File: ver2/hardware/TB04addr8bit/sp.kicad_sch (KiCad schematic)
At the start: 7 parts, among them U32 74AHC04, U39 74HC193, U40 74HC00, U41 74LS32, U42 74AHC04, U43 74LS08

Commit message: ver2: レジスタファイル(RS00/RS01)とルート配線・発振回路定数を追加
- clk_rst: 74HC4060発振のRf=10M/Rs=220K/C=22p×2に確定
- RS00/RS01: R0-R7の具体回路(74HC161×4+74LS253×4)を追加
  ※図面は74LS253だがシンボル都合で実装はHC(74HC253)
- ルート: 書込デコード/読出セレクト/RegAddrSrc MUX/データ入出力の
  外側グルーを配線(DI/DOa/DOb/Reg_WE0-7/sel_a)
- PC_mAddrは作業中(Reg_WE8-11未結線)

Co-Authored-By: Claude Opus 4.8 <noreply@anthropic.com>
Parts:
- removed U32: 74AHC04, symbol 74xx:74AHC04
- removed unit 1 of U42
- added U16: 74HC00, Package_DIP:DIP-14_W7.62mm_Socket, symbol 74xx:74HC00
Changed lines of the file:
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@@
+	)
+	(symbol
+		(lib_id "74xx:74HC00")
+		(at 205.74 147.32 0)
+		(mirror y)
+		(unit 2)
+		(body_style 1)
+		(exclude_from_sim no)
+		(in_bom yes)
+		(on_board yes)
+		(in_pos_files yes)
+		(dnp no)
+		(property "Reference" "U16"
+			(at 205.7483 138.43 0)
+			(show_name no)
+			(do_not_autoplace no)
+			(effects
+				(font
+					(size 1.27 1.27)
+				)
+			)
+		)
+		(property "Value" "74HC00"
+			(at 205.7483 140.97 0)
+			(show_name no)
+			(do_not_autoplace no)
+			(effects
+				(font
+					(size 1.27 1.27)
+				)
+			)
+		)
+		(property "Footprint" "Package_DIP:DIP-14_W7.62mm_Socket"
+			(at 205.74 147.32 0)
+			(hide yes)
+			(show_name no)
+			(do_not_autoplace no)
+			(effects
+				(font
+					(size 1.27 1.27)
+				)
+			)
+		)
+		(property "Datasheet" "http://www.ti.com/lit/gpn/sn74hc00"
+			(at 205.74 147.32 0)
+			(hide yes)
+			(show_name no)
+			(do_not_autoplace no)
+			(effects
+				(font
+					(size 1.27 1.27)
+				)
+			)
+		)
+		(property "Description" "quad 2-input NAND gate"
+			(at 205.74 147.32 0)
+			(hide yes)
+			(show_name no)
+			(do_not_autoplace no)
+			(effects
+				(font
+					(size 1.27 1.27)
+				)
+			)
+		)
+		(pin "1"
+		)
+		(pin "2"
+		)
+		(pin "3"
+		)
+		(pin "9"
+		)
+		(pin "12"
+		)
+		(pin "4"
+		)
+		(pin "5"
+		)
+		(pin "6"
+		)
+		(pin "10"
+		)
+		(pin "8"
+		)
+		(pin "14"
+		)
+		(pin "7"
+		)
+		(pin "11"
+		)
+		(pin "13"
+		)
+		(instances
+			(project "TB04addr8bit"
+				(path "/d176c79b-dced-4d01-bcec-7dfd676fcfc2/49a9e3a4-2acb-465c-a9e5-4345d5d7643a"
+					(reference "U16")
+					(unit 2)
+				)
+			)
+		)
 	)
 	(symbol
@@
 	)
 	(symbol
+		(lib_id "74xx:74HC00")
+		(at 182.88 147.32 0)
+		(mirror y)
+		(unit 1)
+		(body_style 1)
+		(exclude_from_sim no)
+		(in_bom yes)
+		(on_board yes)
+		(in_pos_files yes)
+		(dnp no)
+		(property "Reference" "U16"
+			(at 182.8883 138.43 0)
+			(show_name no)
+			(do_not_autoplace no)
+			(effects
+				(font
+					(size 1.27 1.27)
+				)
+			)
+		)
+		(property "Value" "74HC00"
+			(at 182.8883 140.97 0)
+			(show_name no)
+			(do_not_autoplace no)
+			(effects
+				(font
+					(size 1.27 1.27)
+				)
+			)
+		)
+		(property "Footprint" "Package_DIP:DIP-14_W7.62mm_Socket"
+			(at 182.88 147.32 0)
+			(hide yes)
+			(show_name no)
+			(do_not_autoplace no)
+			(effects
+				(font
+					(size 1.27 1.27)
+				)
+			)
+		)
+		(property "Datasheet" "http://www.ti.com/lit/gpn/sn74hc00"
+			(at 182.88 147.32 0)
+			(hide yes)
+			(show_name no)
+			(do_not_autoplace no)
+			(effects
+				(font
+					(size 1.27 1.27)
+				)
+			)
+		)
+		(property "Description" "quad 2-input NAND gate"
+			(at 182.88 147.32 0)
+			(hide yes)
+			(show_name no)
+			(do_not_autoplace no)
+			(effects
+				(font
+					(size 1.27 1.27)
+				)
+			)
+		)
+		(pin "1"
+		)
+		(pin "2"
+		)
+		(pin "3"
+		)
+		(pin "9"
+		)
+		(pin "12"
+		)
+		(pin "4"
+		)
+		(pin "5"
+		)
+		(pin "6"
+		)
+		(pin "10"
+		)
+		(pin "8"
+		)
+		(pin "14"
+		)
+		(pin "7"
+		)
+		(pin "11"
+		)
+		(pin "13"
+		)
+		(instances
+			(project "TB04addr8bit"
+				(path "/d176c79b-dced-4d01-bcec-7dfd676fcfc2/49a9e3a4-2acb-465c-a9e5-4345d5d7643a"
+					(reference "U16")
+					(unit 1)
+				)
+			)
+		)
+	)
+	(symbol
 		(lib_id "74xx:74AHC04")
 		(at 276.86 63.5 0)
@@
 	)
 	(symbol
-		(lib_id "74xx:74AHC04")
-		(at 255.27 34.29 0)
-		(unit 1)
-		(body_style 1)
-		(exclude_from_sim no)
-		(in_bom yes)
-		(on_board yes)
-		(in_pos_files yes)
-		(dnp no)
-		(fields_autoplaced yes)
-		(property "Reference" "U42"
-			(at 255.27 25.4 0)
-			(show_name no)
-			(do_not_autoplace no)
-			(effects
-				(font
-					(size 1.27 1.27)
-				)
-			)
-		)
-		(property "Value" "74AHC04"
-			(at 255.27 27.94 0)
-			(show_name no)
-			(do_not_autoplace no)
-			(effects
-				(font
-					(size 1.27 1.27)
-				)
-			)
-		)
-		(property "Footprint" ""
-			(at 255.27 34.29 0)
-			(hide yes)
-			(show_name no)
-			(do_not_autoplace no)
-			(effects
-				(font
-					(size 1.27 1.27)
-				)
-			)
-		)
-		(property "Datasheet" "https://assets.nexperia.com/documents/data-sheet/74AHC_AHCT04.pdf"
-			(at 255.27 34.29 0)
-			(hide yes)
-			(show_name no)
-			(do_not_autoplace no)
-			(effects
-				(font
-					(size 1.27 1.27)
-				)
-			)
-		)
-		(property "Description" "Hex Inverter"
-			(at 255.27 34.29 0)
-			(hide yes)
-			(show_name no)
-			(do_not_autoplace no)
-			(effects
-				(font
-					(size 1.27 1.27)
-				)
-			)
-		)
-		(pin "6"
-		)
-		(pin "10"
-		)
-		(pin "9"
-		)
-		(pin "12"
-		)
-		(pin "13"
-		)
-		(pin "11"
-		)
-		(pin "1"
-		)
-		(pin "3"
-		)
-		(pin "7"
-		)
-		(pin "2"
-		)
-		(pin "14"
-		)
-		(pin "5"
-		)
-		(pin "4"
-		)
-		(pin "8"
-		)
-		(instances
-			(project "TB04addr8bit"
-				(path "/d176c79b-dced-4d01-bcec-7dfd676fcfc2/49a9e3a4-2acb-465c-a9e5-4345d5d7643a"
-					(reference "U42")
-					(unit 1)
-				)
-			)
-		)
-	)
-	(symbol
 		(lib_id "74xx:74HC00")
 		(at 204.47 120.65 0)
@@
 				)
 			)
-		)
-	)
-	(symbol
-		(lib_id "74xx:74AHC04")
-		(at 222.25 120.65 0)
-		(unit 5)
-		(body_style 1)
-		(exclude_from_sim no)
-		(in_bom yes)
-		(on_board yes)
-		(in_pos_files yes)
-		(dnp no)
-		(fields_autoplaced yes)
-		(property "Reference" "U32"
-			(at 222.25 111.76 0)
-			(show_name no)
-			(do_not_autoplace no)
-			(effects
-				(font
-					(size 1.27 1.27)
-				)
-			)
-		)
-		(property "Value" "74AHC04"
-			(at 222.25 114.3 0)
-			(show_name no)
-			(do_not_autoplace no)
-			(effects
-				(font
-					(size 1.27 1.27)
-				)
-			)
-		)
-		(property "Footprint" ""
-			(at 222.25 120.65 0)
-			(hide yes)
-			(show_name no)
-			(do_not_autoplace no)
-			(effects
-				(font
-					(size 1.27 1.27)
-				)
-			)
-		)
-		(property "Datasheet" "https://assets.nexperia.com/documents/data-sheet/74AHC_AHCT04.pdf"
-			(at 222.25 120.65 0)
-			(hide yes)
-			(show_name no)
-			(do_not_autoplace no)
-			(effects
-				(font
-					(size 1.27 1.27)
-				)
-			)
-		)
-		(property "Description" "Hex Inverter"
-			(at 222.25 120.65 0)
-			(hide yes)
-			(show_name no)
-			(do_not_autoplace no)
-			(effects
-				(font
-					(size 1.27 1.27)
-				)
-			)
-		)
-		(pin "5"
-		)
-		(pin "1"
-		)
-		(pin "2"
-		)
-		(pin "3"
-		)
-		(pin "9"
-		)
-		(pin "13"
-		)
-		(pin "8"
-		)
-		(pin "10"
-		)
-		(pin "6"
-		)
-		(pin "4"
-		)
-		(pin "11"
-		)
-		(pin "14"
-		)
-		(pin "7"
-		)
-		(pin "12"
-		)
-		(instances
-			(project "TB04addr8bit"
-				(path "/d176c79b-dced-4d01-bcec-7dfd676fcfc2/49a9e3a4-2acb-465c-a9e5-4345d5d7643a"
-					(reference "U32")
-					(unit 5)
-				)
-			)

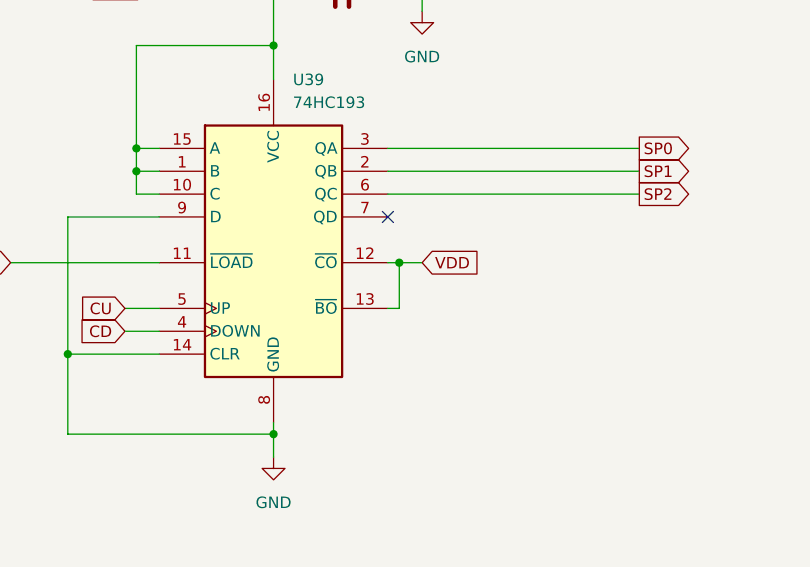
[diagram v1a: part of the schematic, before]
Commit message: ver2: PC_mAddr中心に回路図の配線を更新
7/18のコミット以降の結線作業を反映。部品・ラベルの増減はなく、
配線(wire)とジャンクションの変更のみ。
- PC_mAddr.kicad_sch: 配線36箇所
- sp.kicad_sch / ROM_ALU.kicad_sch / ルートシート: 数箇所ずつ
- TB04addr8bit.kicad_pro: KiCAD 10がERC重要度・last_pathsの
  既定値を追記したもの(設定の書き戻しで設計内容の変化ではない)

なおこの状態のネットリストを ai-review で出力してレビュー済み。
要修正5件と残作業は ver2/DEVLOG.md(2026-08-10)に記録した(未着手)。

Co-Authored-By: Claude Opus 5 <noreply@anthropic.com>
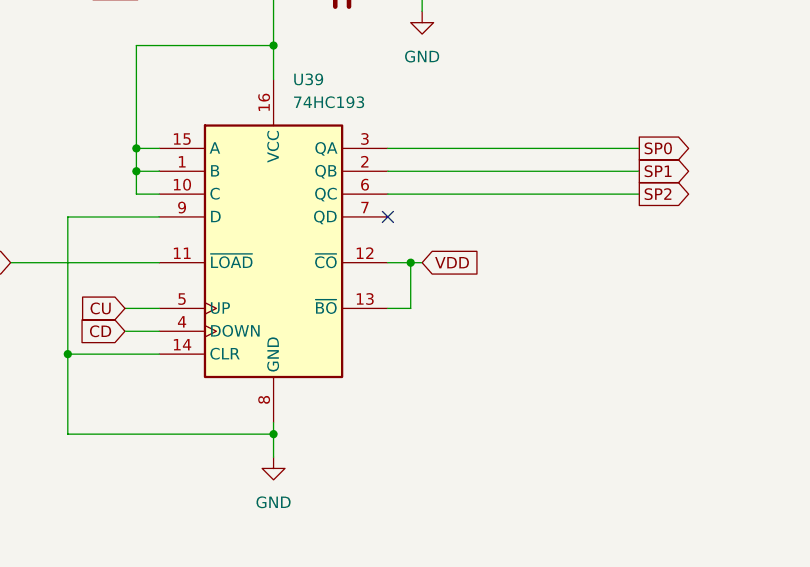
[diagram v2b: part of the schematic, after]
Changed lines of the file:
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@@
+	)
+	(junction
+		(at 123.19 71.12)
+		(diameter 0)
+		(color 0 0 0 0)
 	)
 	(junction
@@
 	(junction
 		(at 107.95 46.99)
-		(diameter 0)
-		(color 0 0 0 0)
-	)
-	(junction
-		(at 121.92 71.12)
 		(diameter 0)
 		(color 0 0 0 0)
@@
 	(wire
 		(pts
-			(xy 120.65 71.12) (xy 121.92 71.12)
-		)
-		(stroke
-			(width 0)
-			(type default)
-		)
-	)
-	(wire
-		(pts
 			(xy 85.09 90.17) (xy 107.95 90.17)
 		)
@@
 	(wire
 		(pts
+			(xy 120.65 71.12) (xy 123.19 71.12)
+		)
+		(stroke
+			(width 0)
+			(type default)
+		)
+	)
+	(wire
+		(pts
 			(xy 92.71 58.42) (xy 95.25 58.42)
 		)
@@
 	(wire
 		(pts
-			(xy 121.92 71.12) (xy 124.46 71.12)
+			(xy 123.19 71.12) (xy 124.46 71.12)
 		)
 		(stroke
@@
 	(wire
 		(pts
+			(xy 120.65 76.2) (xy 123.19 76.2)
+		)
+		(stroke
+			(width 0)
+			(type default)
+		)
+	)
+	(wire
+		(pts
 			(xy 124.46 43.18) (xy 124.46 40.64)
 		)
@@
 	(wire
 		(pts
-			(xy 121.92 76.2) (xy 121.92 71.12)
-		)
-		(stroke
-			(width 0)
-			(type default)
-		)
-	)
-	(wire
-		(pts
 			(xy 59.69 143.51) (xy 81.28 143.51)
 		)
@@
 	(wire
 		(pts
-			(xy 120.65 76.2) (xy 121.92 76.2)
-		)
-		(stroke
-			(width 0)
-			(type default)
-		)
-	)
-	(wire
-		(pts
 			(xy 93.98 40.64) (xy 107.95 40.64)
 		)
@@
 		)
 		(stroke
+			(width 0)
+			(type default)
+		)
+	)
+	(wire
+		(pts
+			(xy 123.19 76.2) (xy 123.19 71.12)
+		)
+		(stroke
